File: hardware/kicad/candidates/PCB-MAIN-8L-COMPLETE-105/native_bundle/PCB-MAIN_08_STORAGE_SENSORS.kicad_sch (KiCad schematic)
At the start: 44 parts, among them J12 MEM2052-00-195-00-A, J13 504050-0291, U12 SDCIT2/32GB, U2 W25Q512JVFIQ, U23 4 channel 0.5 pF ESD, U24 4 channel 0.5 pF ESD, U3 LIS2DW12TR, U4 STTS22HTR

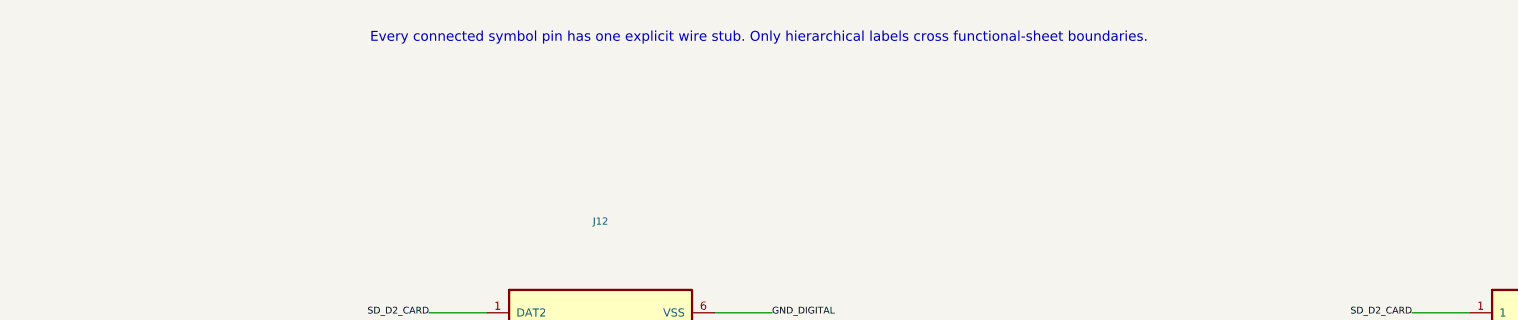
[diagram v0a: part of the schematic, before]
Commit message: PCB-MAIN Rev B: bilingual schematic notes and PDF
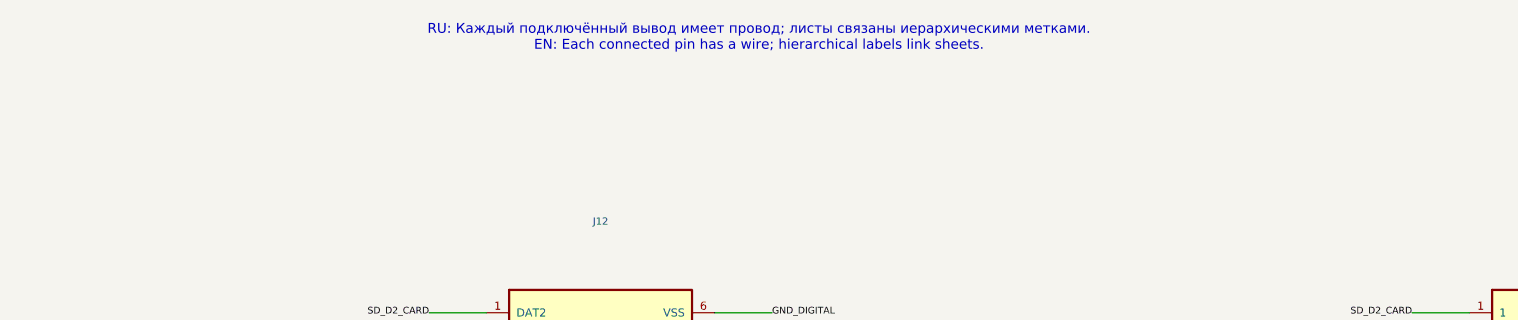
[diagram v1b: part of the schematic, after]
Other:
- note added: "RU: Каждый подключённый вывод имеет провод; листы связаны иерархическими метками. EN: Each connected pin has a wire; hierarchical labels link sheets."
- note removed: "Every connected symbol pin has one explicit wire stub. Only hierarchical labels cross functional-sheet boundaries."
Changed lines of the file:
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@@
     (stroke (width 0.0))
   )
-  (text "Every connected symbol pin has one explicit wire stub. Only hierarchical labels cross functional-sheet boundaries."
+  (text "RU: Каждый подключённый вывод имеет провод; листы связаны иерархическими метками.\nEN: Each connected pin has a wire; hierarchical labels link sheets."
     (at 297.0 12.7 0)
     (effects (font (size 1.1 1.1)))
